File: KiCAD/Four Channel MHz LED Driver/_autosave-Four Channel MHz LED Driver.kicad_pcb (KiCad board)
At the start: 2 copper layers, 100 x 100 mm, 92 parts, among them J1 Barrel_Jack_Switch, J10 Conn_01x24_Female, J2 Conn_01x02_Female, J3 8P8C_Shielded_x4, J4 Conn_01x03_Male, J5 Conn_01x03_Female, J6 Conn_01x08_Female, J7 Conn_01x03_Female, J8 Conn_01x05_Female, J9 Conn_01x24_Female, M1 Fan_4pin, Q1 SUM70060E, SW1 Pushbutton_with_LED, SW2 Pushbutton_with_LED, SW3 Pushbutton_with_LED, SW4 Pushbutton_with_LED, SW5 SW_SPDT, U1 12V boost, U10 ASSR-1218, U11 ASSR-1218, U12 Teensy3.6, U2 SN74LV4T125PWR, U3 DPBW06F-05, U4 TMUX1204DGSR, U5 BDJ0GA5WEFJ-E2, U6 ADP7182AUJZ-1.8-R7, U7 LT6200CS8-10, U8 ASSR-1218, U9 ASSR-1218

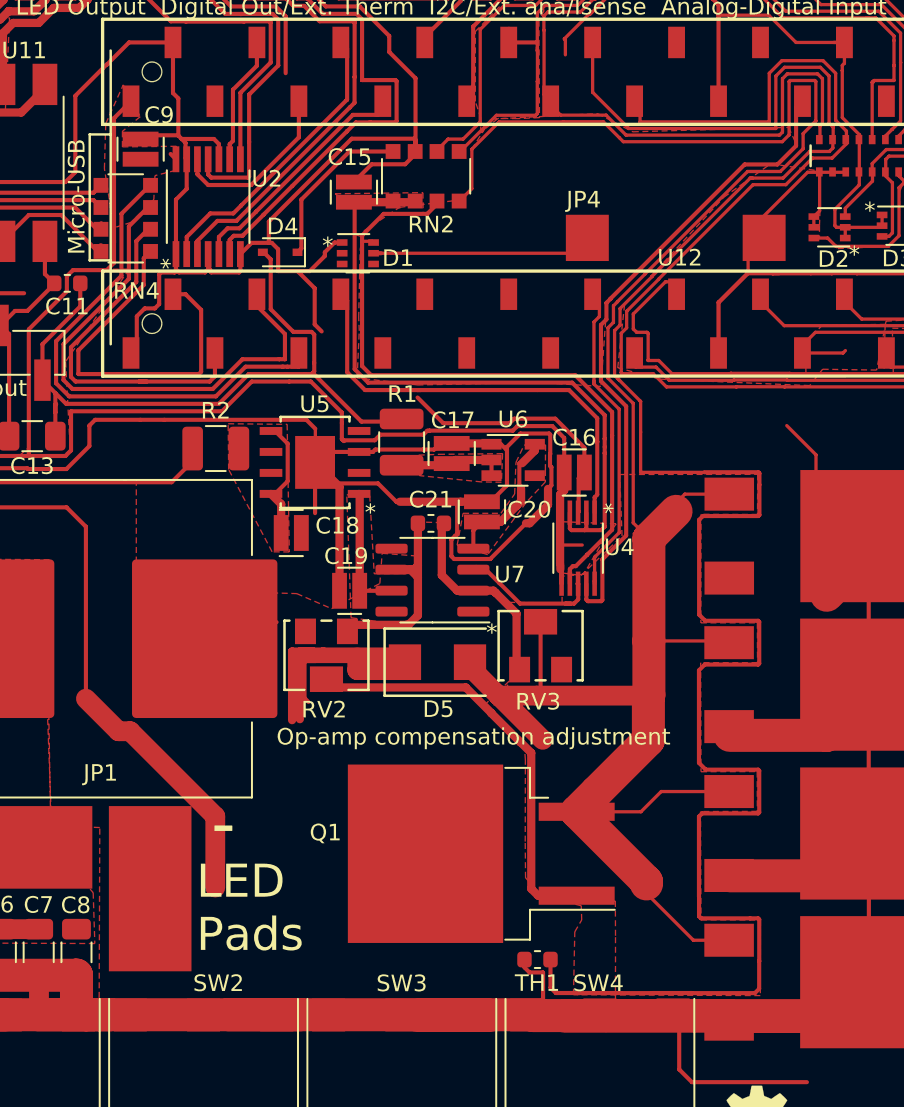
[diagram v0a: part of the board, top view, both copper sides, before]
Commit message: Better grounding for third electrolytic cap
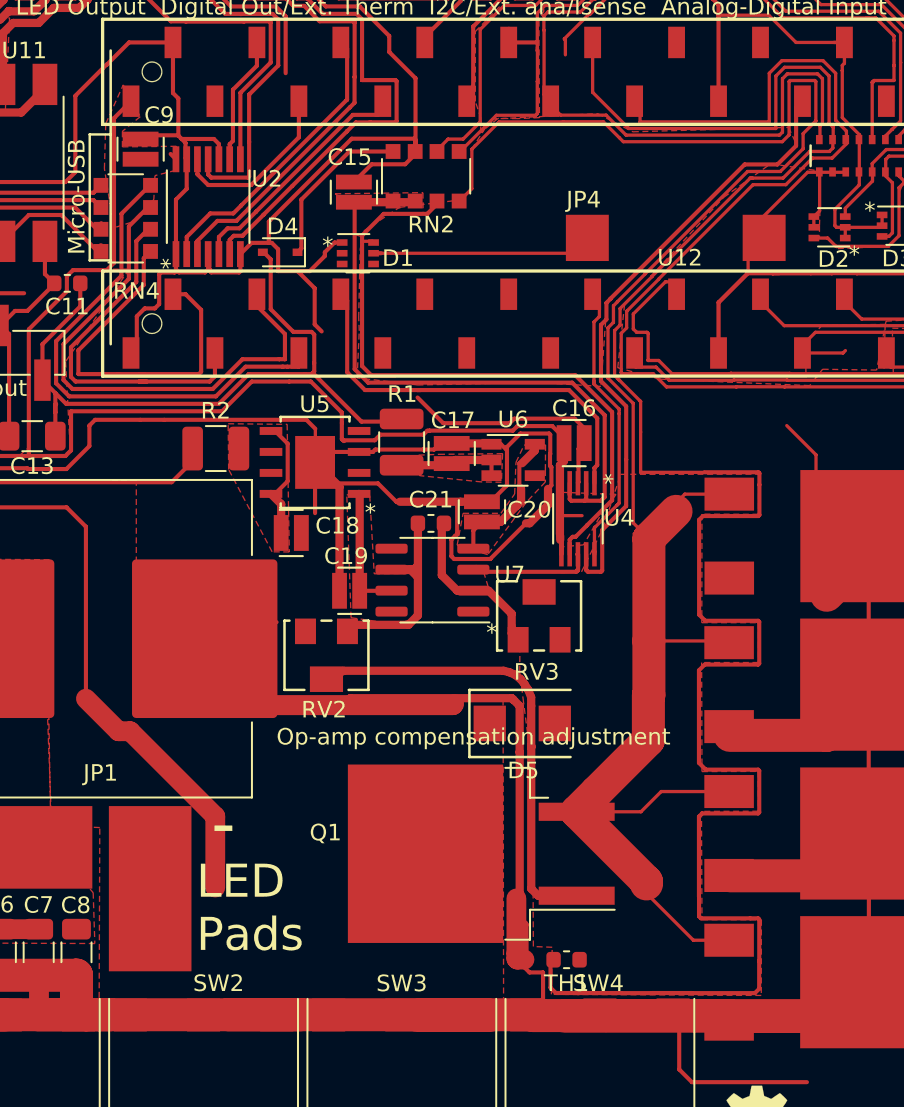
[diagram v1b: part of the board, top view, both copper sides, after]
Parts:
- moved D5 6.33 mm to (98.0, 84.6)
- moved RV3 1.81 mm to (99.0, 78.1)
- moved C16 1.78 mm to (101.1, 67.6)
- moved U4 1.78 mm to (101.4, 72.2)
- moved TH1 1.76 mm to (100.7, 98.9)
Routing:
- net GND: track 1123.9 -> 1179.4 mm
- net /LED-: track 169.4 -> 139.5 mm
- net /Isense: track 138.0 -> 117.8 mm
- net Net-(Q1-Pad1): track 25.3 -> 29.1 mm
- net Net-(C21-Pad2): track 12.2 -> 10.1 mm
- net /5V: track 102.4 -> 100.6 mm
- net /Interline_PWM: track 27.1 -> 25.4 mm
- net /external_analog: track 42.0 -> 40.2 mm
- net /-0.25V_analog: track 45.0 -> 43.2 mm
- net /internal_analog: track 39.6 -> 37.9 mm
- net /Analog_select: track 19.5 -> 17.9 mm
